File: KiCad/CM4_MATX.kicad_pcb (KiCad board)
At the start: 2 copper layers, 244 x 244 mm, 0 parts

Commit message: placed mounting holes as per specification
(0,0) on top left
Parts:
- added C1: 27pF, Capacitor_SMD:C_0402_1005Metric, F.Cu at (-76.8, -17.0)
- added C10: 100n, Capacitor_SMD:C_0402_1005Metric, F.Cu at (-82.5, -17.0)
- added C11: 100n, Capacitor_SMD:C_0402_1005Metric, F.Cu at (-166.6, 8.25)
- added C12: 100n, Capacitor_SMD:C_0402_1005Metric, F.Cu at (-137.8, -19.1)
- added C2: 27pF, Capacitor_SMD:C_0402_1005Metric, F.Cu at (-42.0, -25.6)
- added C3: 10u, Capacitor_SMD:C_0805_2012Metric, F.Cu at (-101.5, 2.56)
- added C4: 10u, Capacitor_SMD:C_0805_2012Metric, F.Cu at (-88.9, -12.7)
- added C5: 100n, Capacitor_SMD:C_0402_1005Metric, F.Cu at (-82.3, -15.1)
- added C6: 100n, Capacitor_SMD:C_0402_1005Metric, F.Cu at (-42.0, -27.5)
- added C7: 100n, Capacitor_SMD:C_0402_1005Metric, F.Cu at (-79.6, -17.0)
- added C8: 100n, Capacitor_SMD:C_0402_1005Metric, F.Cu at (-97.8, 4.12)
- added C9: 100n, Capacitor_SMD:C_0402_1005Metric, F.Cu at (-75.1, -21.8)
- added H1: MountingHole, MountingHole:MountingHole_3.2mm_M3, F.Cu at (237.5, 237.5)
- added H2: MountingHole, MountingHole:MountingHole_3.2mm_M3, F.Cu at (34.3, 165.1)
- added H3: MountingHole, MountingHole:MountingHole_3.2mm_M3, F.Cu at (80.0, 10.2)
- added H4: MountingHole, MountingHole:MountingHole_3.2mm_M3, F.Cu at (237.5, 165.1)
- added H5: MountingHole, MountingHole:MountingHole_3.2mm_M3, F.Cu at (34.3, 10.2)
- added H6: MountingHole, MountingHole:MountingHole_3.2mm_M3, F.Cu at (80.0, 165.1)
- added H7: MountingHole, MountingHole:MountingHole_3.2mm_M3, F.Cu at (14.0, 165.1)
- added H8: MountingHole, MountingHole:MountingHole_3.2mm_M3, F.Cu at (237.5, 10.2)
- added H9: MountingHole, MountingHole:MountingHole_3.2mm_M3, F.Cu at (80.0, 237.5)
- added IC1: USB2517-JZX, CM4_MATX:QFN50P900X900X100-65N-D, F.Cu at (-86.4, -2.52)
- added IC2: PI7C9X2G404SLBFDE, CM4_MATX:QFP40P1600X1600X160-129N, F.Cu at (-105.2, 49.4)
- added J10: 72309-8014BLF, CM4_MATX:723098014BLF, F.Cu at (-104.5, -25.3)
- added J11: SS-52100-002, CM4_MATX:SS52100002, F.Cu at (-105.0, -4.91)
- added J12: Conn_02x05_Odd_Even, Connector_PinHeader_2.54mm:PinHeader_2x05_P2.54mm_Vertical, F.Cu at (-108.6, 3.38)
- added J13: Conn_02x05_Odd_Even, Connector_PinHeader_2.54mm:PinHeader_2x05_P2.54mm_Vertical, F.Cu at (-88.8, -26.7)
- added J2: THD-02-R, Connector_PinHeader_2.54mm:PinHeader_2x02_P2.54mm_Vertical, F.Cu at (-144.1, -17.7)
- added J3: Conn_01x22_Female, Connector_FFC-FPC:Hirose_FH12-22S-0.5SH_1x22-1MP_P0.50mm_Horizontal, F.Cu at (-159.0, -2.71)
- added J4: Conn_01x22_Female, Connector_FFC-FPC:Hirose_FH12-22S-0.5SH_1x22-1MP_P0.50mm_Horizontal, F.Cu at (-181.9, 30.6)
- added J5: Conn_01x22_Female, Connector_FFC-FPC:Hirose_FH12-22S-0.5SH_1x22-1MP_P0.50mm_Horizontal, F.Cu at (-137.4, -25.5)
- added J6: Conn_01x22_Female, Connector_FFC-FPC:Hirose_FH12-22S-0.5SH_1x22-1MP_P0.50mm_Horizontal, F.Cu at (-200.1, 30.6)
- added J7: 1888811-1, CM4_MATX:TE_1888811-1, F.Cu at (-157.3, -20.4)
- added J8: 10018783-11200TLF, CM4_MATX:1001878410200TLF, F.Cu at (-129.0, 45.4)
- added J9: 39-28-1243, CM4_MATX:SHDR24W125P550X420_2X12_5160X960X1310P, F.Cu at (-205.7, 42.8)
- added Module1: ComputeModule4, CM4_MATX:Raspberry-Pi-4-Compute-Module, F.Cu at (-205.1, 23.1)
- added R1: 2.2K 1%, Resistor_SMD:R_0402_1005Metric, F.Cu at (-85.2, -13.2)
- added R2: 2.2K 1%, Resistor_SMD:R_0402_1005Metric, F.Cu at (-109.5, 16.9)
- added R3: 36K 1%, Resistor_SMD:R_0402_1005Metric, F.Cu at (-102.3, 5.06)
- added R4: 36K 1%, Resistor_SMD:R_0402_1005Metric, F.Cu at (-97.8, 2.05)
- added R5: 36K 1%, Resistor_SMD:R_0402_1005Metric, F.Cu at (-86.8, -10.2)
- added R6: 36K 1%, Resistor_SMD:R_0402_1005Metric, F.Cu at (-89.7, -10.2)
- added R7: 2.2K 1%, Resistor_SMD:R_0402_1005Metric, F.Cu at (-162.2, 3.71)
- added R8: 2.2K 1%, Resistor_SMD:R_0402_1005Metric, F.Cu at (-148.4, -5.24)
- added U1: FSUSB42MX, Package_SO:MSOP-10_3x3mm_P0.5mm, F.Cu at (-80.2, -20.4)
- added U2: RT9742SNGV, Package_TO_SOT_SMD:SOT-23, F.Cu at (-165.8, 4.99)
- added Y1: 24MHz, Crystal:Crystal_SMD_HC49-SD, F.Cu at (-50.8, -25.4)

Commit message: Preliminary component placement and PCB PDF
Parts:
- added J1: 10104110-0001LF, _LibLoader:101041100001LF, F.Cu at (25.0, 97.0)
- IC1: footprint CM4_MATX:QFN50P900X900X100-65N-D -> _LibLoader:QFN50P900X900X100-65N-D
- IC2: footprint CM4_MATX:QFP40P1600X1600X160-129N -> _LibLoader:QFP40P1600X1600X160-129N
- J10: footprint CM4_MATX:723098014BLF -> _LibLoader:723098014BLF
- J11: footprint CM4_MATX:SS52100002 -> _LibLoader:SS52100002
- J8: footprint CM4_MATX:1001878410200TLF -> _LibLoader:1001878410200TLF
- J9: footprint CM4_MATX:SHDR24W125P550X420_2X12_5160X960X1310P -> _LibLoader:SHDR24W125P550X420_2X12_5160X960X1310P
- moved J9 468.9 mm to (255.0, 130.0), turned to 90 degrees
- moved J11 445.8 mm to (260.0, 251.0), turned to -90 degrees
- moved J12 432.9 mm to (259.0, 232.0)
- moved C8 432.1 mm to (254.0, 255.0), turned to 90 degrees
- moved J13 424.7 mm to (259.0, 217.0)
- moved C10 416.7 mm to (256.0, 226.0)
- moved C9 414.2 mm to (256.0, 227.0)
- moved J6 368.2 mm to (165.7, 72.7)
- moved C3 363.3 mm to (247.1, 105.0)
- moved C4 359.7 mm to (251.1, 105.0)
- moved J4 327.4 mm to (144.0, 61.0)
- moved R7 326.9 mm to (153.3, 89.8)
- moved R8 318.7 mm to (155.8, 89.8)
- moved J5 315.5 mm to (166.0, 61.0)
- moved J2 313.6 mm to (153.0, 82.5)
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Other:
- board text added: "Camera Connectors"
- board text added: "Display Connectors"
- board text added: "NOTE: COMPONENT PLACEMENT NOT FINAL"

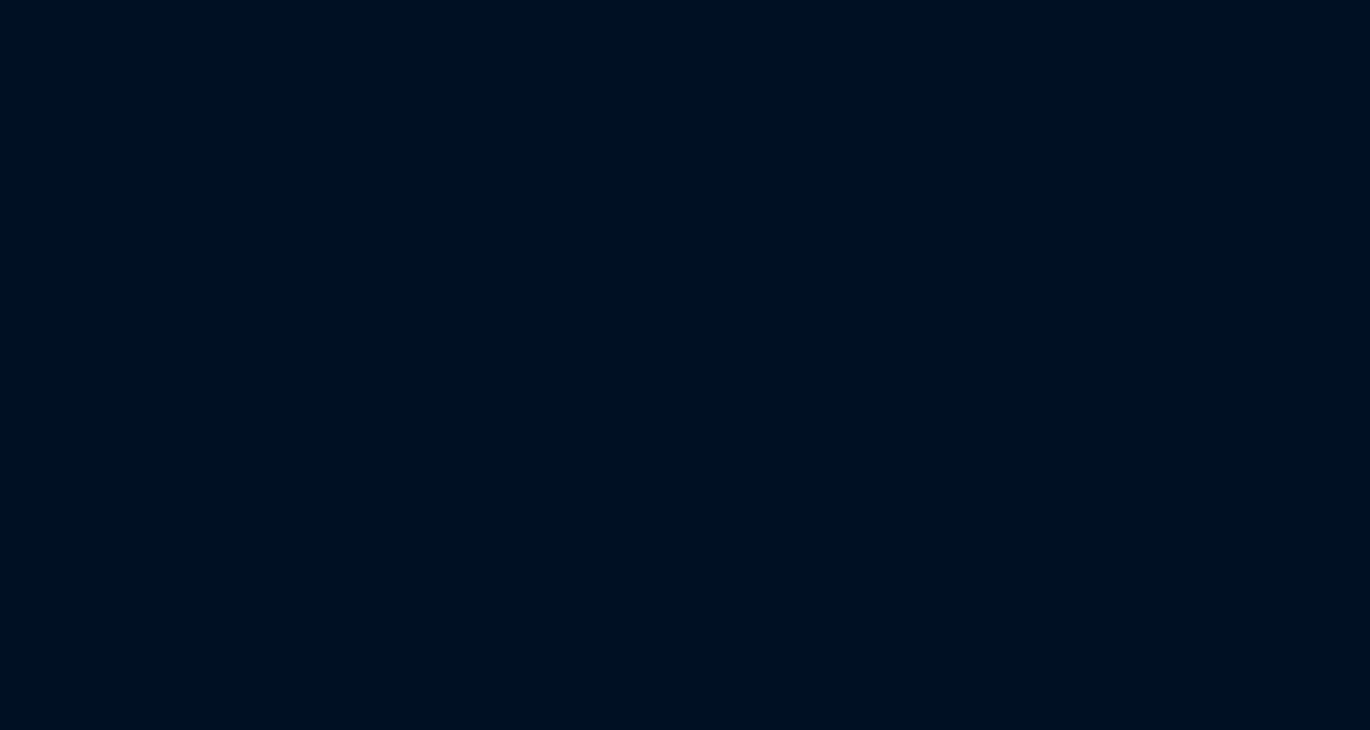
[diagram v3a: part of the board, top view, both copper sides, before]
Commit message: added CM4_FanCRTL to CM4_MATX
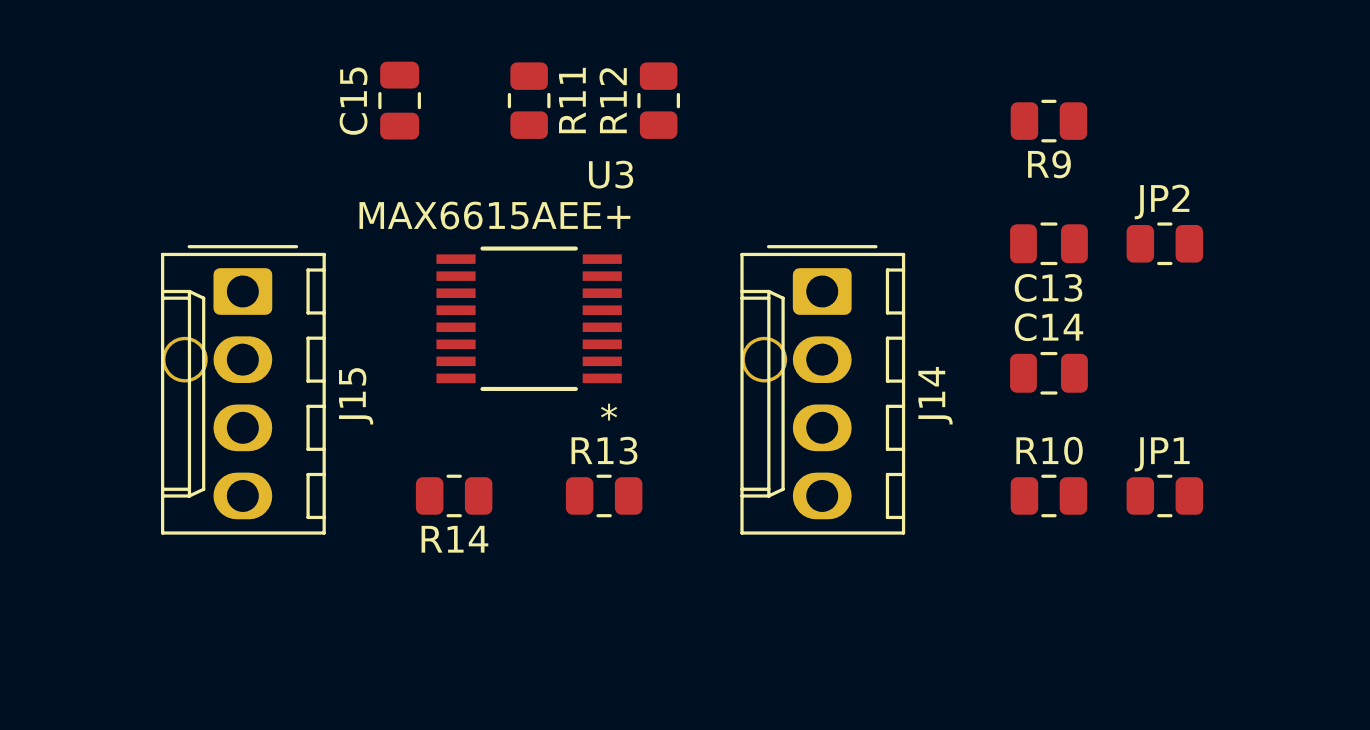
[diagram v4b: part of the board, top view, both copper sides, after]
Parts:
- added C13: C100p, CM4_MATX:C_0805_2012Metric, F.Cu at (153.2, -23.9)
- added C14: C100p, CM4_MATX:C_0805_2012Metric, F.Cu at (153.2, -19.1)
- added C15: C0.1u, CM4_MATX:C_0805_2012Metric, F.Cu at (129.0, -29.2)
- added J14: KK-254-470531000, CM4_MATX:Molex_KK-254_AE-6410-04A_1x04_P2.54mm_Vertical, F.Cu at (144.8, -22.1)
- added J15: KK-254-470531000, CM4_MATX:Molex_KK-254_AE-6410-04A_1x04_P2.54mm_Vertical, F.Cu at (123.2, -22.1)
- added JP1: SolderJumper_2_Open, CM4_MATX:R_0805_2012Metric, F.Cu at (157.5, -14.5)
- added JP2: SolderJumper_2_Open, CM4_MATX:R_0805_2012Metric, F.Cu at (157.5, -23.9)
- added R10: R1.6k, CM4_MATX:R_0805_2012Metric, F.Cu at (153.2, -14.5)
- added R11: R10k, CM4_MATX:R_0805_2012Metric, F.Cu at (133.9, -29.2)
- added R12: R10k, CM4_MATX:R_0805_2012Metric, F.Cu at (138.7, -29.2)
- added R13: R4.7k, CM4_MATX:R_0805_2012Metric, F.Cu at (136.7, -14.5)
- added R14: R4.7k, CM4_MATX:R_0805_2012Metric, F.Cu at (131.1, -14.5)
- added R9: R1.6k, CM4_MATX:R_0805_2012Metric, F.Cu at (153.2, -28.4)
- added U3: MAX6615AEE+, CM4_MATX:MAX6615AEE&plus_, F.Cu at (133.9, -21.1)
